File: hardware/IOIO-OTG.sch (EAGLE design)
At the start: 58 parts, among them Q1 IRLML2244, Q2 2N7002PW, Q3 AO3404A, U1 PIC24FJ256GB206, U14 SWITCH_SPDT, U2 TPS62133RGTT, U3 VREG_MIC5216

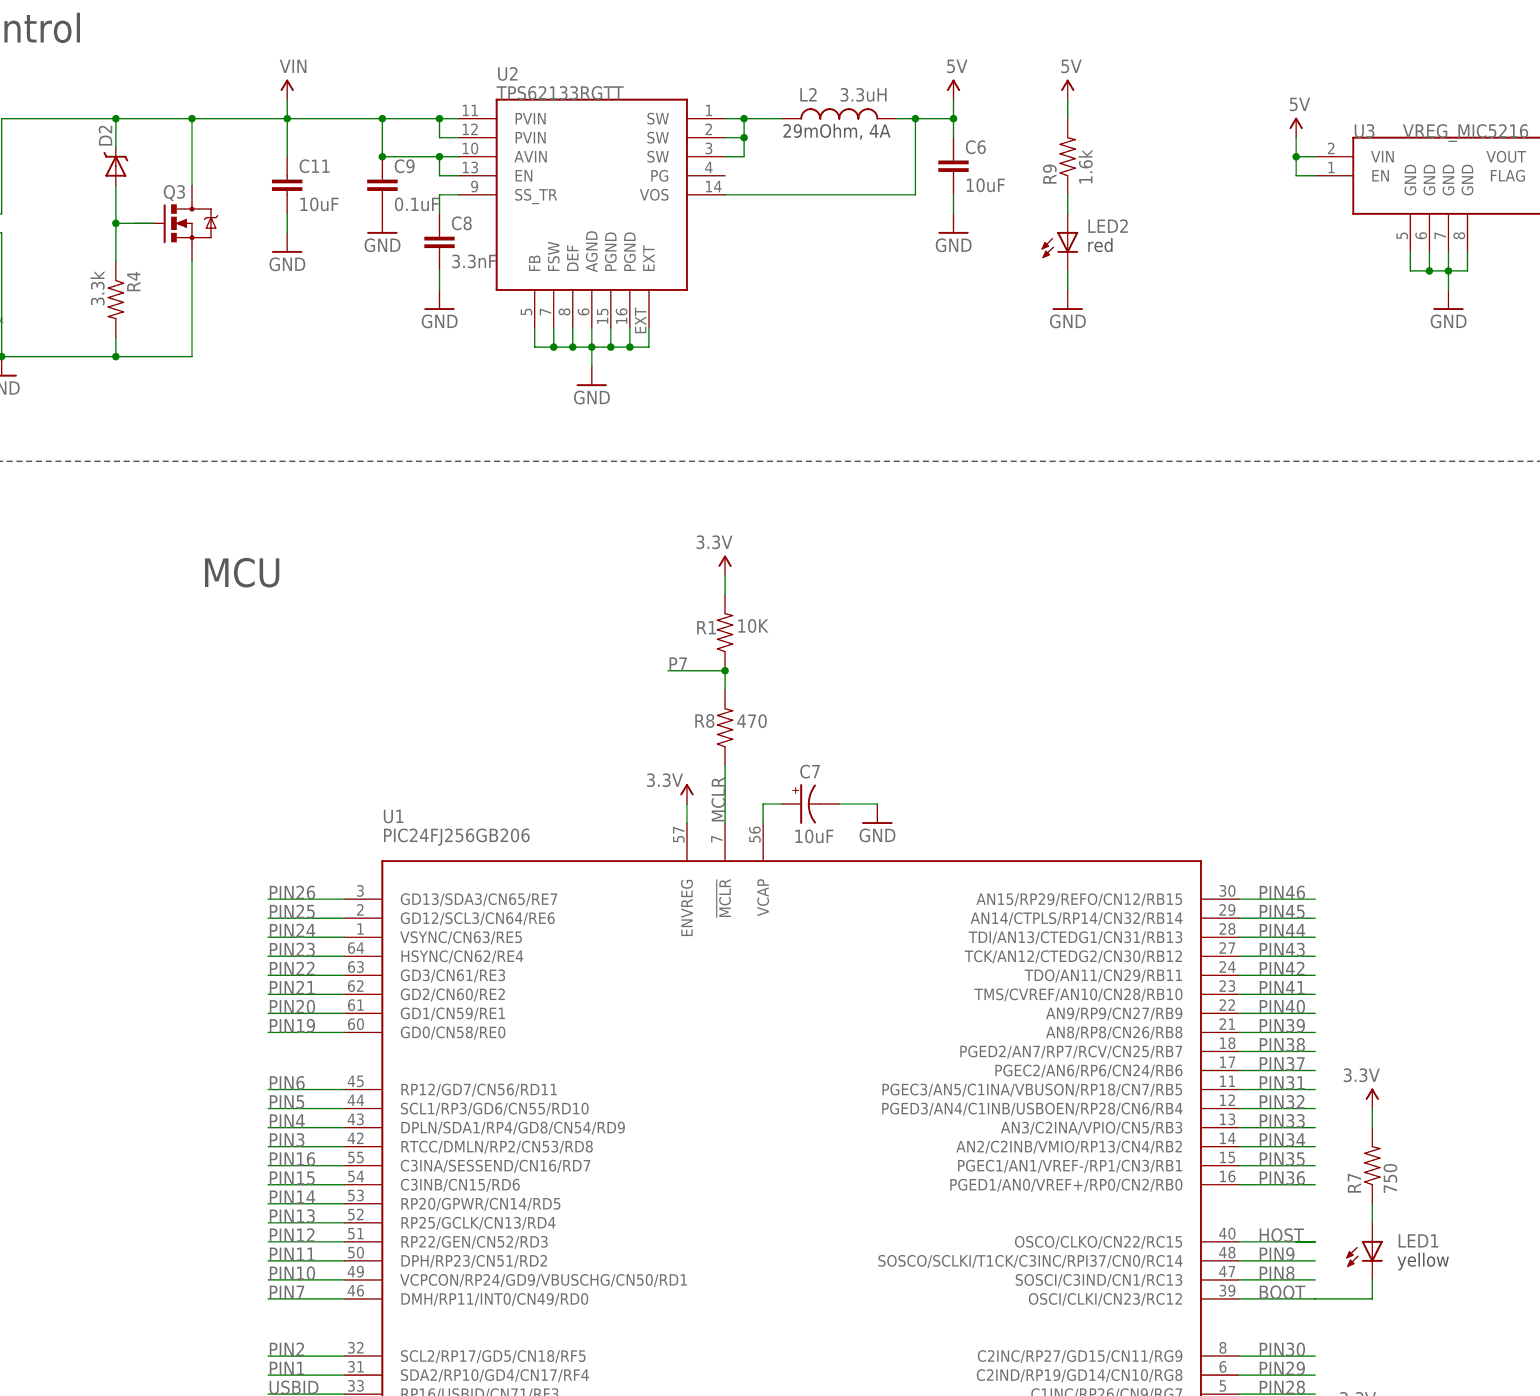
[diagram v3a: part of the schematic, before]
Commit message: All remaining 0402 passives bumped to 0603
all components had slight shift in X/Y coordinates. Components near the
TPS6124 also requires some shifting. Included an "original" and "moved
to 0603" screen shot of design for review.
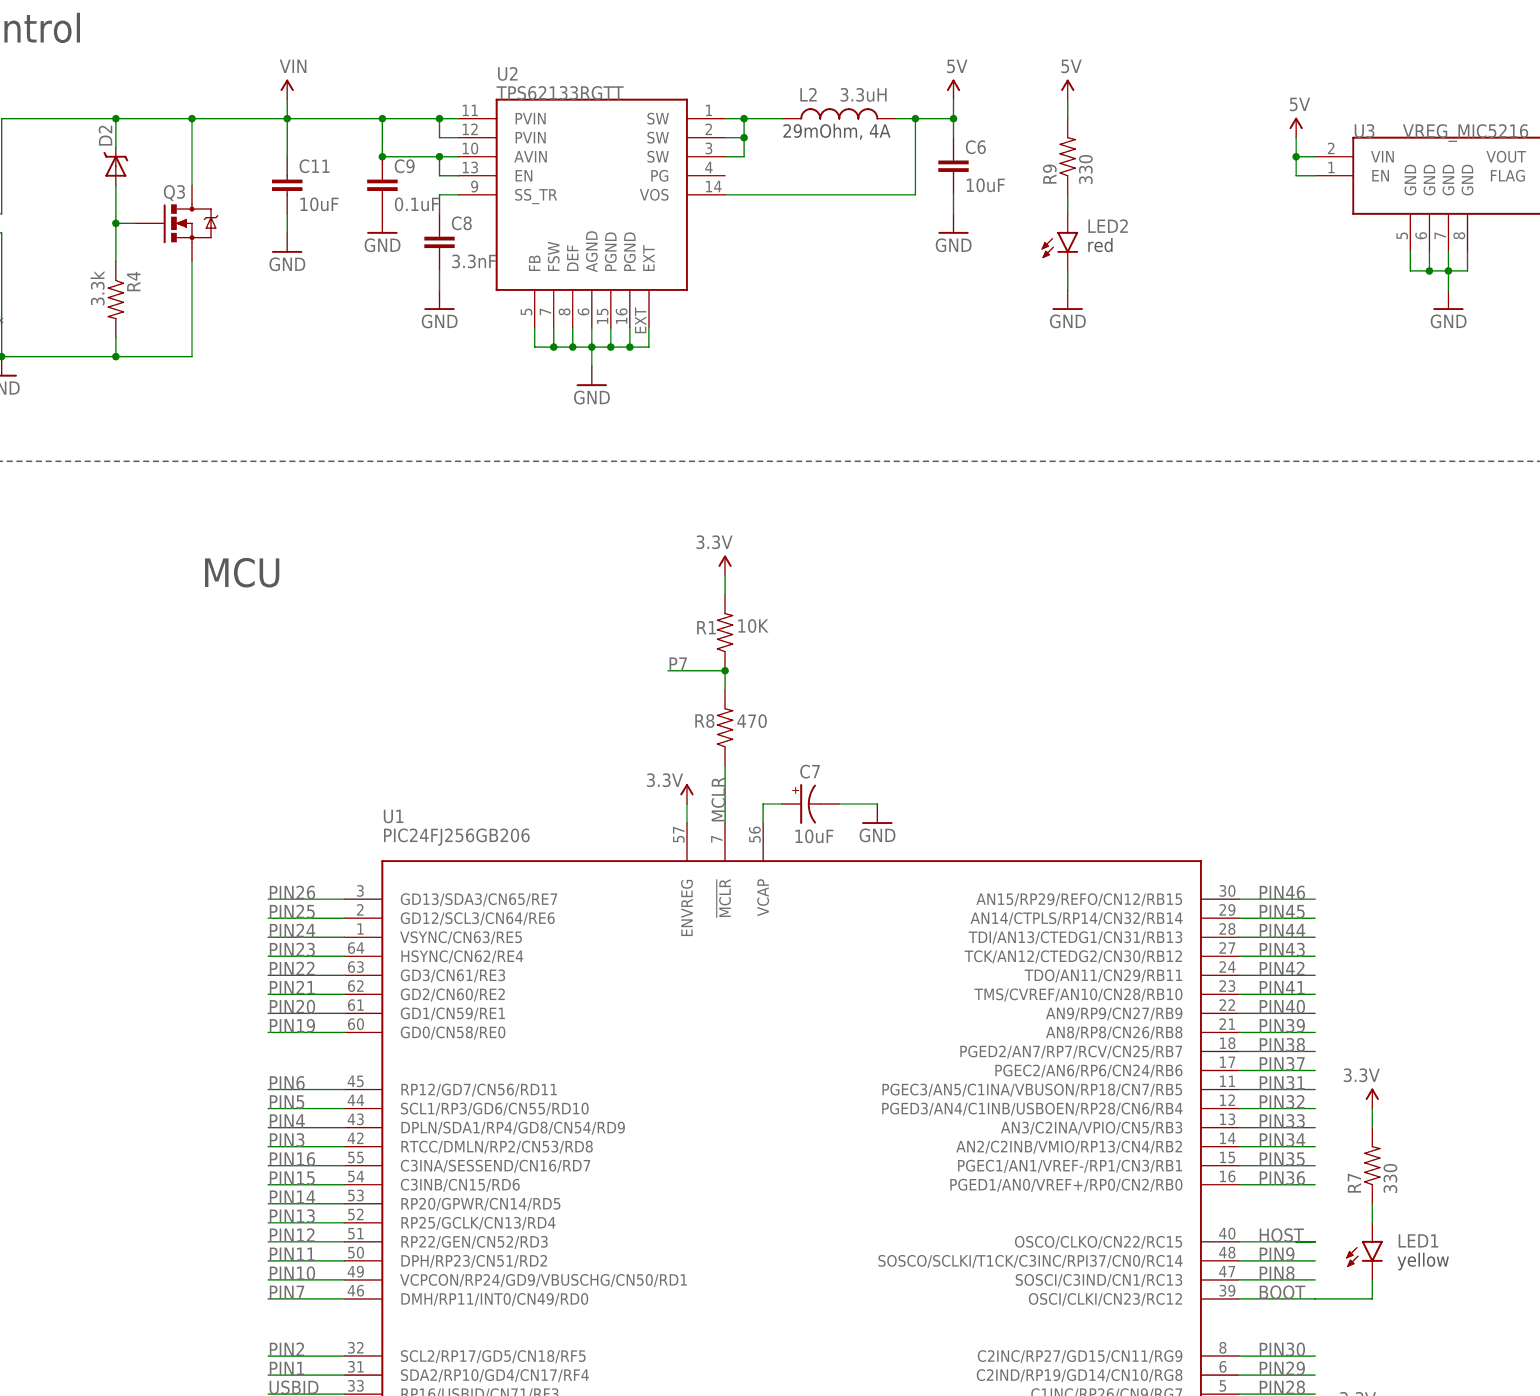
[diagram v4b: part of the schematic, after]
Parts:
- C2, C5, C9: device SparkFun:CAP0402-CAP -> SparkFun-Capacitors:0.1UF-25V(+80/-20%)(0603)
- C8: device SparkFun:CAP0402-CAP -> SparkFun-Capacitors:3.3NF-100V-10%(0603)
- LED1: value LY L29K-J1K2-26-Z -> Yellow; device SparkFun:LED0603 -> SparkFun-LED:LED-YELLOW0603
- LED2: value LS L29K-G1J2-1-Z -> RED; device SparkFun:LED0603 -> SparkFun-LED:LED-RED0603
- R2: device SparkFun:RESISTOR0402-RES -> SparkFun-Resistors:100KOHM-1/10W-1%(0603)
- R3: device SparkFun-Electromechanical:TRIMPOTTRIMPOT-5MM -> SparkFun-Electromechanical:TRIMPOTRES-11156
- R4: device SparkFun:RESISTOR0402-RES -> SparkFun-Resistors:3.3KOHM1/10W1%(0603)
- R7: value 750 -> 330; device SparkFun:RESISTOR0402-RES -> SparkFun-Resistors:330OHM1/10W1%(0603)
- R9: value 1.6k -> 330; device SparkFun:RESISTOR0402-RES -> SparkFun-Resistors:330OHM1/10W1%(0603)
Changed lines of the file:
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@@
 <part name="U1" library="SparkFun-DigitalIC" deviceset="PIC24FXXXDAX06" device="" value="PIC24FJ256GB206"/>
 <part name="C1" library="SparkFun-Capacitors" deviceset="0.1UF-25V(+80/-20%)(0603)" device="" value="0.1uF"/>
-<part name="C2" library="SparkFun" deviceset="CAP" device="0402-CAP" value="0.1uF"/>
+<part name="C2" library="SparkFun-Capacitors" deviceset="0.1UF-25V(+80/-20%)(0603)" device="" value="0.1uF"/>
 <part name="C3" library="SparkFun-Capacitors" deviceset="0.1UF-25V(+80/-20%)(0603)" device="" value="0.1uF"/>
 <part name="C4" library="SparkFun-Capacitors" deviceset="0.1UF-25V(+80/-20%)(0603)" device="" value="0.1uF"/>
@@
 <part name="R1" library="SparkFun-Resistors" deviceset="10KOHM-1/10W-1%(0603)" device="0603" value="10K"/>
 <part name="P+6" library="SparkFun" deviceset="3.3V" device=""/>
-<part name="C5" library="SparkFun" deviceset="CAP" device="0402-CAP" value="0.1uF"/>
+<part name="C5" library="SparkFun-Capacitors" deviceset="0.1UF-25V(+80/-20%)(0603)" device="" value="0.1uF"/>
 <part name="GND7" library="SparkFun" deviceset="GND" device=""/>
 <part name="P+7" library="SparkFun" deviceset="3.3V" device=""/>
@@
 <part name="U$5" library="SparkFun" deviceset="5V" device=""/>
 <part name="JP4" library="SparkFun" deviceset="M03" device="PTH" value="5V"/>
-<part name="R7" library="SparkFun" deviceset="RESISTOR" device="0402-RES" value="750"/>
+<part name="R7" library="SparkFun-Resistors" deviceset="330OHM1/10W1%(0603)" device="" value="330"/>
 <part name="P+11" library="SparkFun" deviceset="3.3V" device=""/>
 <part name="R8" library="SparkFun-Resistors" deviceset="470OHM1/10W1%(0603)" device="" value="470"/>
@@
 <part name="JP12" library="SparkFun" deviceset="STAND-OFF" device=""/>
 <part name="JP13" library="SparkFun" deviceset="STAND-OFF" device=""/>
-<part name="LED1" library="SparkFun" deviceset="LED" device="0603" value="LY L29K-J1K2-26-Z"/>
+<part name="LED1" library="SparkFun-LED" deviceset="LED-YELLOW" device="0603" value="Yellow"/>
 <part name="JP5" library="SparkFun" deviceset="M03" device="PTH"/>
-<part name="R9" library="SparkFun" deviceset="RESISTOR" device="0402-RES" value="1.6k"/>
-<part name="LED2" library="SparkFun" deviceset="LED" device="0603" value="LS L29K-G1J2-1-Z"/>
+<part name="R9" library="SparkFun-Resistors" deviceset="330OHM1/10W1%(0603)" device="" value="330"/>
+<part name="LED2" library="SparkFun-LED" deviceset="LED-RED" device="0603" value="RED"/>
 <part name="GND6" library="SparkFun" deviceset="GND" device=""/>
 <part name="JP15" library="SparkFun" deviceset="M01" device="PTH"/>
@@
 <attribute name="PART#" value="0ZCA0075FF2G"/>
 </part>
-<part name="R2" library="SparkFun" deviceset="RESISTOR" device="0402-RES" value="100k"/>
+<part name="R2" library="SparkFun-Resistors" deviceset="100KOHM-1/10W-1%(0603)" device="" value="100k"/>
 <part name="C10" library="SparkFun-Passives" deviceset="CAP_POL" device="1206" value="10uF">
 <attribute name="PART#" value="TAJA106K016RNJ"/>
@@
 <attribute name="PART#" value="LMK212BJ106KG-T"/>
 </part>
-<part name="C8" library="SparkFun" deviceset="CAP" device="0402-CAP" value="3.3nF"/>
+<part name="C8" library="SparkFun-Capacitors" deviceset="3.3NF-100V-10%(0603)" device="" value="3.3nF"/>
 <part name="C11" library="SparkFun-Passives" deviceset="CAP" device="1210" value="10uF">
 <attribute name="PART#" value="UMK325C7106MM-T"/>
@@
 <part name="JP1" library="SparkFun" deviceset="M03" device="PTH" value="VIN"/>
 <part name="JP3" library="SparkFun" deviceset="M01" device="PTH"/>
-<part name="R3" library="SparkFun-Electromechanical" deviceset="TRIMPOT" device="TRIMPOT-5MM" value="TS53YL502MR10">
+<part name="R3" library="SparkFun-Electromechanical" deviceset="TRIMPOT" device="RES-11156" value="TS53YL502MR10">
 <attribute name="PART#" value="TS53YL502MR10"/>
 </part>
@@
 <attribute name="PART#" value="DMN3404L"/>
 </part>
-<part name="R4" library="SparkFun" deviceset="RESISTOR" device="0402-RES" value="3.3k"/>
+<part name="R4" library="SparkFun-Resistors" deviceset="3.3KOHM1/10W1%(0603)" device="" value="3.3k"/>
 <part name="D2" library="IOIO-OTG" deviceset="SPARKFUN-DISCRETESEMI_DIODE-SCHOTTKY" device="" value="DZ2J160M0L">
 <attribute name="PART#" value="DZ2J150M0L"/>
 </part>
-<part name="C9" library="SparkFun" deviceset="CAP" device="0402-CAP" value="0.1uF"/>
+<part name="C9" library="SparkFun-Capacitors" deviceset="0.1UF-25V(+80/-20%)(0603)" device="" value="0.1uF"/>
 <part name="GND20" library="SparkFun" deviceset="GND" device=""/>
 <part name="JP18" library="SparkFun-Connectors" deviceset="USB_MICROB_PLUG" device="CONN-11752"/>
@@
 <net name="N$12" class="0">
 <segment>
-<wire x1="53.34" y1="222.25" x2="50.8" y2="222.25" width="0.1524" layer="91"/>
 <wire x1="50.8" y1="222.25" x2="48.26" y2="222.25" width="0.1524" layer="91"/>
 <wire x1="48.26" y1="222.25" x2="48.26" y2="227.33" width="0.1524" layer="91"/>

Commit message: Moved to v22 in sch/copper, updated frame in SCH
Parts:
- removed U$1: CREATIVE_COMMONS, SparkFun-Aesthetics:CREATIVE_COMMONS
- added FRAME2: FRAME-LEDGER, SparkFun-Aesthetics:FRAME-LEDGER
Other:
- note added: "V22"
- moved on the sheet: C1, C10, C11, C2, C3, C4, C5, C6, C7, C8, C9, D1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

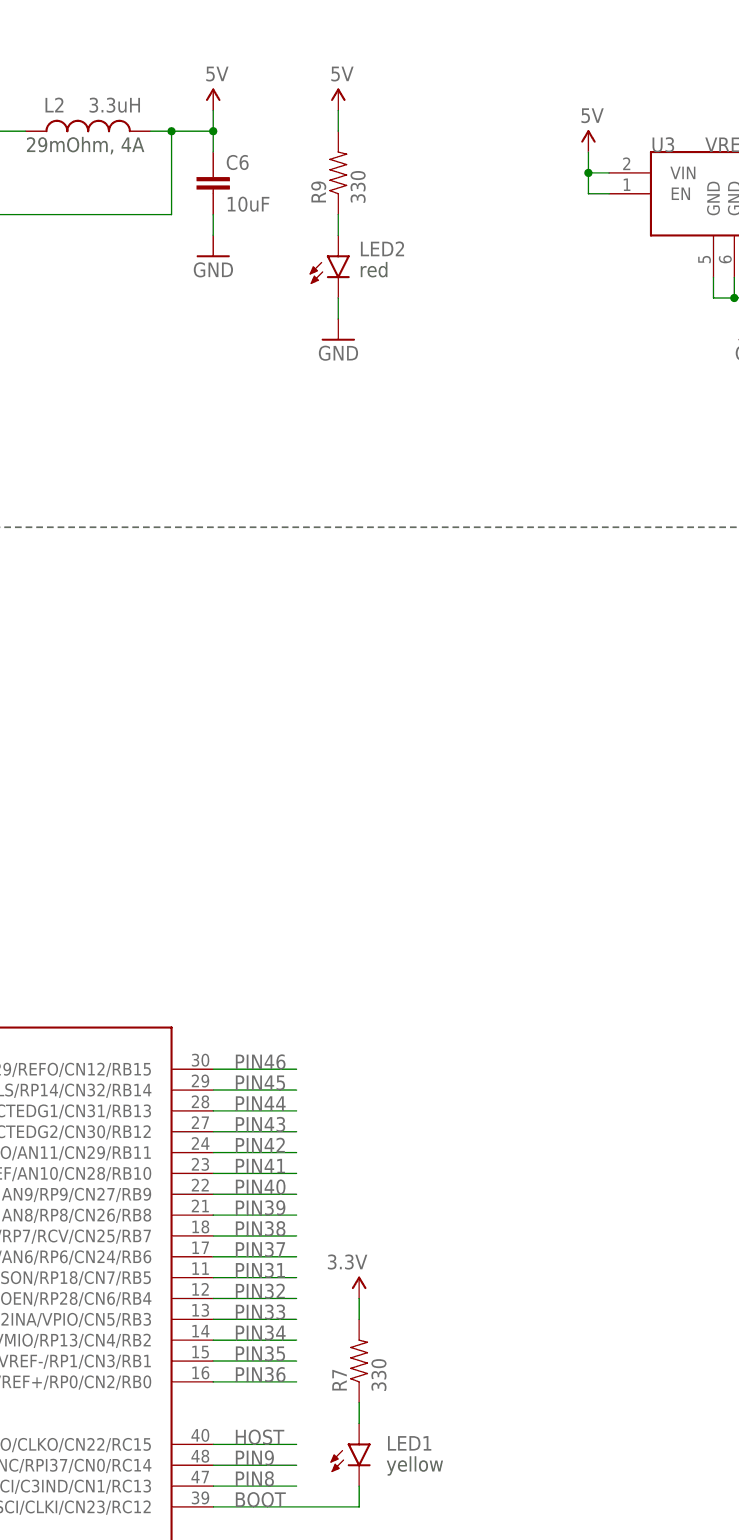
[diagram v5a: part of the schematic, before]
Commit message: Restored back to 1.6K and 750 ohm LED resistors
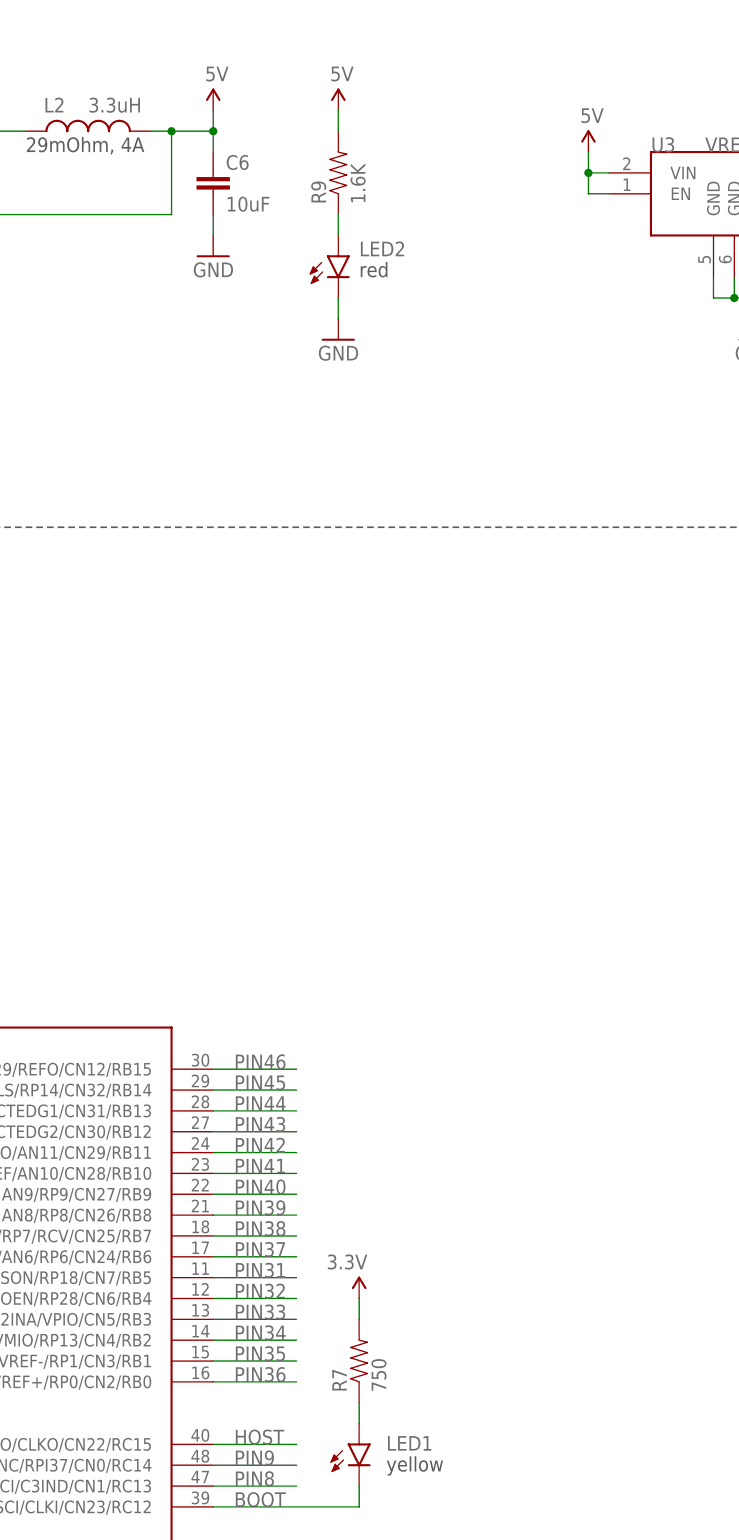
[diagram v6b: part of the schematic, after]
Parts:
- LED1: device SparkFun-LED:LED-YELLOW0603 -> SparkFun-LED:LED-YELLOW0603-SMART
- LED2: value RED -> Red; device SparkFun-LED:LED-RED0603 -> SparkFun-LED:LED-RED0603-SMART
- R7: value 330 -> 750; device SparkFun-Resistors:330OHM1/10W1%(0603) -> SparkFun-Resistors:750OHM1/10W1%(0603)0603
- R9: value 330 -> 1.6K; device SparkFun-Resistors:330OHM1/10W1%(0603) -> SparkFun-Resistors:1.6KOHM-1/10W-1%(0603)0603
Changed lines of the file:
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@@
 <part name="U$5" library="SparkFun" deviceset="5V" device=""/>
 <part name="JP4" library="SparkFun" deviceset="M03" device="PTH" value="5V"/>
-<part name="R7" library="SparkFun-Resistors" deviceset="330OHM1/10W1%(0603)" device="" value="330"/>
+<part name="R7" library="SparkFun-Resistors" deviceset="750OHM1/10W1%(0603)" device="0603" value="750"/>
 <part name="P+11" library="SparkFun" deviceset="3.3V" device=""/>
 <part name="R8" library="SparkFun-Resistors" deviceset="470OHM1/10W1%(0603)" device="" value="470"/>
@@
 <part name="JP12" library="SparkFun" deviceset="STAND-OFF" device=""/>
 <part name="JP13" library="SparkFun" deviceset="STAND-OFF" device=""/>
-<part name="LED1" library="SparkFun-LED" deviceset="LED-YELLOW" device="0603" value="Yellow"/>
+<part name="LED1" library="SparkFun-LED" deviceset="LED-YELLOW" device="0603-SMART" value="Yellow"/>
 <part name="JP5" library="SparkFun" deviceset="M03" device="PTH"/>
-<part name="R9" library="SparkFun-Resistors" deviceset="330OHM1/10W1%(0603)" device="" value="330"/>
-<part name="LED2" library="SparkFun-LED" deviceset="LED-RED" device="0603" value="RED"/>
+<part name="R9" library="SparkFun-Resistors" deviceset="1.6KOHM-1/10W-1%(0603)" device="0603" value="1.6K"/>
+<part name="LED2" library="SparkFun-LED" deviceset="LED-RED" device="0603-SMART" value="Red"/>
 <part name="GND6" library="SparkFun" deviceset="GND" device=""/>
 <part name="JP15" library="SparkFun" deviceset="M01" device="PTH"/>
